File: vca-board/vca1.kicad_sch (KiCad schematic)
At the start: 8 parts, among them U1 SSI2164-Split, U3 TL074

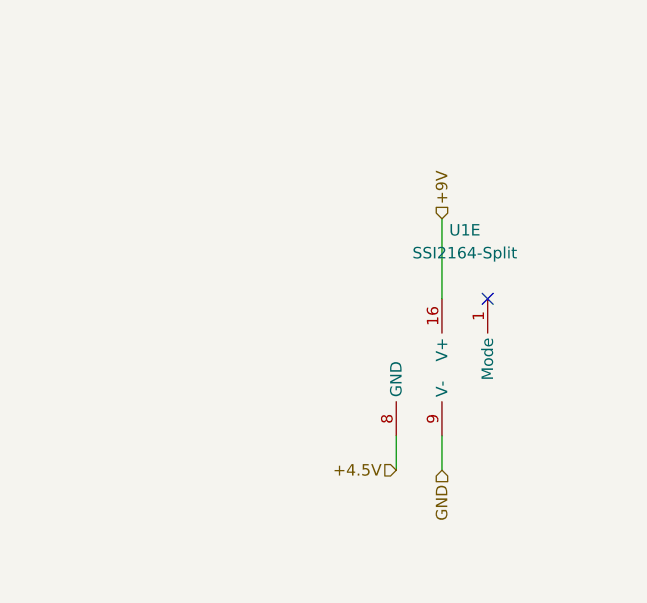
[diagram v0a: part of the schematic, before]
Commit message: VCA components linked
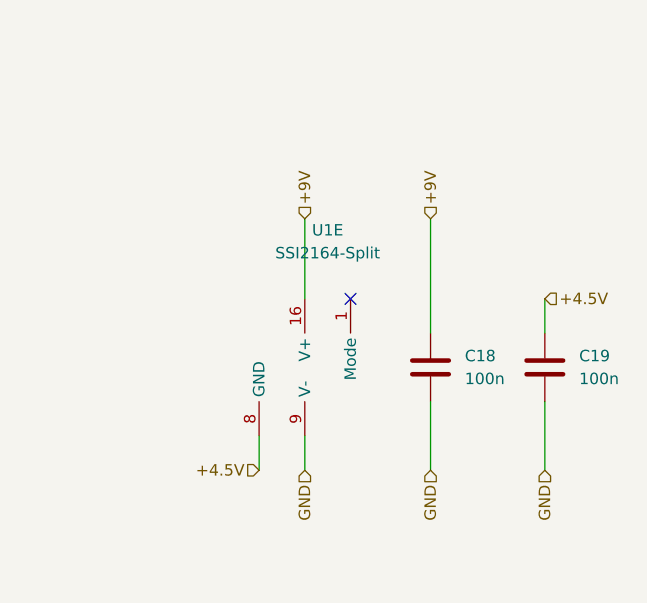
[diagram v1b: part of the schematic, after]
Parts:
- added C18, C19: 100n, Capacitor_SMD:C_0603_1608Metric_Pad1.08x0.95mm_HandSolder, symbol Device:C
- C7: footprint (none) -> Capacitor_SMD:C_0603_1608Metric_Pad1.08x0.95mm_HandSolder; LCSC (none) -> C3012379
- C8: footprint (none) -> Capacitor_SMD:C_0603_1608Metric_Pad1.08x0.95mm_HandSolder; LCSC (none) -> C160903
- R17, R19: LCSC (none) -> C4184
- R18: LCSC (none) -> C22962
- R20: LCSC (none) -> C21190
- U3: footprint (none) -> Package_SO:SOIC-14_3.9x8.7mm_P1.27mm; LCSC (none) -> C6963
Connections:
- net +4.5V: now also C19.2
- net +9V: now also C18.2
- net GND: now also C18.1, C19.1
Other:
- moved on the sheet: U1E
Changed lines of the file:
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@@
   (junction (at 120.65 53.34) (diameter 0) (color 0 0 0 0)
   )
-  (no_connect (at 260.35 58.42))
+  (no_connect (at 245.11 58.42))
   (wire (pts (xy 135.89 66.04) (xy 140.97 66.04))
     (stroke (width 0) (type default) (color 0 0 0 0))
@@
     (stroke (width 0) (type default) (color 0 0 0 0))
   )
+  (wire (pts (xy 266.7 69.85) (xy 266.7 77.47))
+    (stroke (width 0) (type default) (color 0 0 0 0))
+  )
   (wire (pts (xy 90.17 63.5) (xy 96.52 63.5))
     (stroke (width 0) (type default) (color 0 0 0 0))
@@
     (stroke (width 0) (type default) (color 0 0 0 0))
   )
+  (wire (pts (xy 254 69.85) (xy 254 77.47))
+    (stroke (width 0) (type default) (color 0 0 0 0))
+  )
   (wire (pts (xy 124.46 41.91) (xy 120.65 41.91))
     (stroke (width 0) (type default) (color 0 0 0 0))
@@
     (stroke (width 0) (type default) (color 0 0 0 0))
   )
-  (wire (pts (xy 255.27 49.53) (xy 255.27 58.42))
+  (wire (pts (xy 254 49.53) (xy 254 62.23))
+    (stroke (width 0) (type default) (color 0 0 0 0))
+  )
+  (wire (pts (xy 240.03 49.53) (xy 240.03 58.42))
     (stroke (width 0) (type default) (color 0 0 0 0))
   )
@@
     (stroke (width 0) (type default) (color 0 0 0 0))
   )
-  (wire (pts (xy 255.27 73.66) (xy 255.27 77.47))
+  (wire (pts (xy 240.03 73.66) (xy 240.03 77.47))
     (stroke (width 0) (type default) (color 0 0 0 0))
   )
@@
     (stroke (width 0) (type default) (color 0 0 0 0))
   )
-  (wire (pts (xy 250.19 73.66) (xy 250.19 77.47))
+  (wire (pts (xy 234.95 73.66) (xy 234.95 77.47))
+    (stroke (width 0) (type default) (color 0 0 0 0))
+  )
+  (wire (pts (xy 266.7 58.42) (xy 266.7 62.23))
     (stroke (width 0) (type default) (color 0 0 0 0))
   )
@@
     (effects (font (size 1.27 1.27)) (justify right bottom))
   )
-  (hierarchical_label "GND" (shape input) (at 255.27 77.47 270)
-    (effects (font (size 1.27 1.27)) (justify right))
-  )
-  (hierarchical_label "+4.5V" (shape input) (at 250.19 77.47 180)
+  (hierarchical_label "GND" (shape input) (at 240.03 77.47 270)
+    (effects (font (size 1.27 1.27)) (justify right))
+  )
+  (hierarchical_label "GND" (shape input) (at 254 77.47 270)
+    (effects (font (size 1.27 1.27)) (justify right))
+  )
+  (hierarchical_label "+4.5V" (shape input) (at 234.95 77.47 180)
     (effects (font (size 1.27 1.27)) (justify right))
   )
@@
     (effects (font (size 1.27 1.27)) (justify right))
   )
-  (hierarchical_label "+9V" (shape input) (at 255.27 49.53 90)
+  (hierarchical_label "+9V" (shape input) (at 240.03 49.53 90)
     (effects (font (size 1.27 1.27)) (justify left))
   )
@@
     (effects (font (size 1.27 1.27)) (justify right))
   )
+  (hierarchical_label "+4.5V" (shape input) (at 266.7 58.42 0)
+    (effects (font (size 1.27 1.27)) (justify left))
+  )
+  (hierarchical_label "GND" (shape input) (at 266.7 77.47 270)
+    (effects (font (size 1.27 1.27)) (justify right))
+  )
+  (hierarchical_label "+9V" (shape input) (at 254 49.53 90)
+    (effects (font (size 1.27 1.27)) (justify left))
+  )
   (hierarchical_label "VCA1_Out" (shape input) (at 152.4 66.04 0)
     (effects (font (size 1.27 1.27)) (justify left))
@@
       (effects (font (size 1.27 1.27)) hide)
     )
-    (pin "1")
-    (pin "2")
-  )
-  (symbol (lib_id "pedals:SSI2164-Split") (at 257.81 66.04 0) (unit 5)
-    (in_bom yes) (on_board yes) (fields_autoplaced)
-    (property "Reference" "U1" (id 0) (at 257.81 50.8 0))
-    (property "Value" "SSI2164-Split" (id 1) (at 257.81 53.34 0))
-    (property "Footprint" "Package_SO:SOIC-16_3.9x9.9mm_P1.27mm" (id 2) (at 257.81 78.74 0)
-      (effects (font (size 1.27 1.27)) hide)
-    )
-    (property "Datasheet" "https://www.soundsemiconductor.com/downloads/ssi2164datasheet.pdf" (id 3) (at 257.81 76.2 0)
+    (property "LCSC" "C22962" (id 4) (at 90.17 72.39 0)
+      (effects (font (size 1.27 1.27)) hide)
+    )
+    (pin "1")
+    (pin "2")
+  )
+  (symbol (lib_id "pedals:SSI2164-Split") (at 242.57 66.04 0) (unit 5)
+    (in_bom yes) (on_board yes) (fields_autoplaced)
+    (property "Reference" "U1" (id 0) (at 242.57 50.8 0))
+    (property "Value" "SSI2164-Split" (id 1) (at 242.57 53.34 0))
+    (property "Footprint" "Package_SO:SOIC-16_3.9x9.9mm_P1.27mm" (id 2) (at 242.57 78.74 0)
+      (effects (font (size 1.27 1.27)) hide)
+    )
+    (property "Datasheet" "https://www.soundsemiconductor.com/downloads/ssi2164datasheet.pdf" (id 3) (at 242.57 76.2 0)
       (effects (font (size 1.27 1.27)) hide)
     )
@@
       (effects (font (size 1.27 1.27)) hide)
     )
+    (property "LCSC" "C4184" (id 4) (at 80.01 63.5 0)
+      (effects (font (size 1.27 1.27)) hide)
+    )
     (pin "1")
     (pin "2")
@@
       (effects (font (size 1.27 1.27)) hide)
     )
+    (property "LCSC" "C21190" (id 4) (at 144.78 66.04 0)
+      (effects (font (size 1.27 1.27)) hide)
+    )
+    (pin "1")
+    (pin "2")
+  )
+  (symbol (lib_id "Device:C") (at 254 66.04 180) (unit 1)
+    (in_bom yes) (on_board yes) (fields_autoplaced)
+    (property "Reference" "C18" (id 0) (at 257.81 64.7699 0)
+      (effects (font (size 1.27 1.27)) (justify right))
+    )
+    (property "Value" "100n" (id 1) (at 257.81 67.3099 0)
+      (effects (font (size 1.27 1.27)) (justify right))
+    )
+    (property "Footprint" "Capacitor_SMD:C_0603_1608Metric_Pad1.08x0.95mm_HandSolder" (id 2) (at 253.0348 62.23 0)
+      (effects (font (size 1.27 1.27)) hide)
+    )
+    (property "Datasheet" "~" (id 3) (at 254 66.04 0)
+      (effects (font (size 1.27 1.27)) hide)
+    )
+    (property "LCSC" "C76711" (id 4) (at 254 66.04 0)
+      (effects (font (size 1.27 1.27)) hide)
+    )
     (pin "1")
     (pin "2")
@@
     (property "Reference" "C8" (id 0) (at 128.27 34.29 90))
     (property "Value" "100p" (id 1) (at 128.27 36.83 90))
-    (property "Footprint" "" (id 2) (at 124.46 42.8752 0)
+    (property "Footprint" "Capacitor_SMD:C_0603_1608Metric_Pad1.08x0.95mm_HandSolder" (id 2) (at 124.46 42.8752 0)
       (effects (font (size 1.27 1.27)) hide)
     )
     (property "Datasheet" "~" (id 3) (at 128.27 41.91 0)
+      (effects (font (size 1.27 1.27)) hide)
+    )
+    (property "LCSC" "C160903" (id 4) (at 128.27 41.91 0)
+      (effects (font (size 1.27 1.27)) hide)
+    )
+    (pin "1")
+    (pin "2")
+  )
+  (symbol (lib_id "Device:C") (at 266.7 66.04 180) (unit 1)
+    (in_bom yes) (on_board yes) (fields_autoplaced)
+    (property "Reference" "C19" (id 0) (at 270.51 64.7699 0)
+      (effects (font (size 1.27 1.27)) (justify right))
+    )
+    (property "Value" "100n" (id 1) (at 270.51 67.3099 0)
+      (effects (font (size 1.27 1.27)) (justify right))
+    )
+    (property "Footprint" "Capacitor_SMD:C_0603_1608Metric_Pad1.08x0.95mm_HandSolder" (id 2) (at 265.7348 62.23 0)
+      (effects (font (size 1.27 1.27)) hide)
+    )
+    (property "Datasheet" "~" (id 3) (at 266.7 66.04 0)
+      (effects (font (size 1.27 1.27)) hide)
+    )
+    (property "LCSC" "C76711" (id 4) (at 266.7 66.04 0)
       (effects (font (size 1.27 1.27)) hide)
     )
@@
     (property "Reference" "U3" (id 0) (at 128.27 55.88 0))
     (property "Value" "TL074" (id 1) (at 128.27 58.42 0))
-    (property "Footprint" "" (id 2) (at 127 68.58 0)
+    (property "Footprint" "Package_SO:SOIC-14_3.9x8.7mm_P1.27mm" (id 2) (at 127 68.58 0)
       (effects (font (size 1.27 1.27)) hide)
     )
     (property "Datasheet" "http://www.ti.com/lit/ds/symlink/tl071.pdf" (id 3) (at 129.54 71.12 0)
+      (effects (font (size 1.27 1.27)) hide)
+    )
+    (property "LCSC" "C6963" (id 4) (at 128.27 66.04 0)
       (effects (font (size 1.27 1.27)) hide)
     )
@@
       (effects (font (size 1.27 1.27)) hide)
     )
+    (property "LCSC" "C4184" (id 4) (at 128.27 53.34 0)
+      (effects (font (size 1.27 1.27)) hide)
+    )
     (pin "1")
     (pin "2")
@@
       (effects (font (size 1.27 1.27)) (justify right))
     )
-    (property "Footprint" "" (id 2) (at 89.2048 77.47 0)
+    (property "Footprint" "Capacitor_SMD:C_0603_1608Metric_Pad1.08x0.95mm_HandSolder" (id 2) (at 89.2048 77.47 0)
       (effects (font (size 1.27 1.27)) hide)
     )
@@
       (effects (font (size 1.27 1.27)) hide)
     )
+    (property "LCSC" "C3012379" (id 4) (at 90.17 81.28 0)
+      (effects (font (size 1.27 1.27)) hide)
+    )

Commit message: VCA board components placed
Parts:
- R17, R18, R19, R20: footprint (none) -> Resistor_SMD:R_0603_1608Metric_Pad0.98x0.95mm_HandSolder
- renumbered U3 to U4
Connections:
- net +4.5V: now also U4.12 (+); no longer U4.10 (+)
- net SSI1_Out_Sum_In: now also U4.13 (-); no longer U4.9 (-)
- net at C8.1, R19.2, R20.1: now also U4.14; no longer U4.8
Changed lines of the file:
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@@
       (effects (font (size 1.27 1.27)) (justify right))
     )
-    (property "Footprint" "" (id 2) (at 91.948 72.39 90)
+    (property "Footprint" "Resistor_SMD:R_0603_1608Metric_Pad0.98x0.95mm_HandSolder" (id 2) (at 91.948 72.39 90)
       (effects (font (size 1.27 1.27)) hide)
     )
@@
     (property "Reference" "R17" (id 0) (at 80.01 57.15 90))
     (property "Value" "20k" (id 1) (at 80.01 59.69 90))
-    (property "Footprint" "" (id 2) (at 80.01 65.278 90)
+    (property "Footprint" "Resistor_SMD:R_0603_1608Metric_Pad0.98x0.95mm_HandSolder" (id 2) (at 80.01 65.278 90)
       (effects (font (size 1.27 1.27)) hide)
     )
@@
     (property "Reference" "R20" (id 0) (at 144.78 59.69 90))
     (property "Value" "1k" (id 1) (at 144.78 62.23 90))
-    (property "Footprint" "" (id 2) (at 144.78 67.818 90)
+    (property "Footprint" "Resistor_SMD:R_0603_1608Metric_Pad0.98x0.95mm_HandSolder" (id 2) (at 144.78 67.818 90)
       (effects (font (size 1.27 1.27)) hide)
     )
@@
     (pin "2")
   )
-  (symbol (lib_id "Amplifier_Operational:TL074") (at 128.27 66.04 0) (mirror x) (unit 3)
+  (symbol (lib_id "Amplifier_Operational:TL074") (at 128.27 66.04 0) (mirror x) (unit 4)
     (in_bom yes) (on_board yes) (fields_autoplaced)
-    (property "Reference" "U3" (id 0) (at 128.27 55.88 0))
+    (property "Reference" "U4" (id 0) (at 128.27 55.88 0))
     (property "Value" "TL074" (id 1) (at 128.27 58.42 0))
     (property "Footprint" "Package_SO:SOIC-14_3.9x8.7mm_P1.27mm" (id 2) (at 127 68.58 0)
@@
     (property "Reference" "R19" (id 0) (at 128.27 46.99 90))
     (property "Value" "20k" (id 1) (at 128.27 49.53 90))
-    (property "Footprint" "" (id 2) (at 128.27 55.118 90)
+    (property "Footprint" "Resistor_SMD:R_0603_1608Metric_Pad0.98x0.95mm_HandSolder" (id 2) (at 128.27 55.118 90)
       (effects (font (size 1.27 1.27)) hide)
     )

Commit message: Filter board schem done
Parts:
- C7: value 1n -> 1.2n; LCSC C3012379 -> C576816
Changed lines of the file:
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@@
       (effects (font (size 1.27 1.27)) (justify right))
     )
-    (property "Value" "1n" (id 1) (at 93.98 82.5499 0)
+    (property "Value" "1.2n" (id 1) (at 93.98 82.5499 0)
       (effects (font (size 1.27 1.27)) (justify right))
     )
@@
       (effects (font (size 1.27 1.27)) hide)
     )
-    (property "LCSC" "C3012379" (id 4) (at 90.17 81.28 0)
+    (property "LCSC" "C576816" (id 4) (at 90.17 81.28 0)
       (effects (font (size 1.27 1.27)) hide)
     )

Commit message: Remove D from linear VCA + update graphics
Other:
- company: (none) -> Pedal Markt / Andrey Salomatin
- title: (none) -> VCA Board
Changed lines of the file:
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@@
 (kicad_sch (version 20211123) (generator eeschema)
   (paper "A4")
+  (title_block
+    (title "VCA Board")
+    (date "2024-11-07")
+    (rev "v1rev2")
+    (company "Pedal Markt / Andrey Salomatin")
+  )
   (junction (at 120.65 41.91) (diameter 0) (color 0 0 0 0)
   )

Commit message: wip pre-redo orientation
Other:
- company: Pedal Markt / Andrey Salomatin -> Andrey Salomatin / Pedal Markt
- title: VCA Board -> Mag
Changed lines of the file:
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@@
   (paper "A4")
   (title_block
-    (title "VCA Board")
+    (title "Mag")
     (date "2024-11-07")
     (rev "v1rev2")
-    (company "Pedal Markt / Andrey Salomatin")
+    (company "Andrey Salomatin / Pedal Markt")
   )
   (junction (at 120.65 41.91) (diameter 0) (color 0 0 0 0)
